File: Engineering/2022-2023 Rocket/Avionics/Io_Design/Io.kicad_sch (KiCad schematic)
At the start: 9 parts

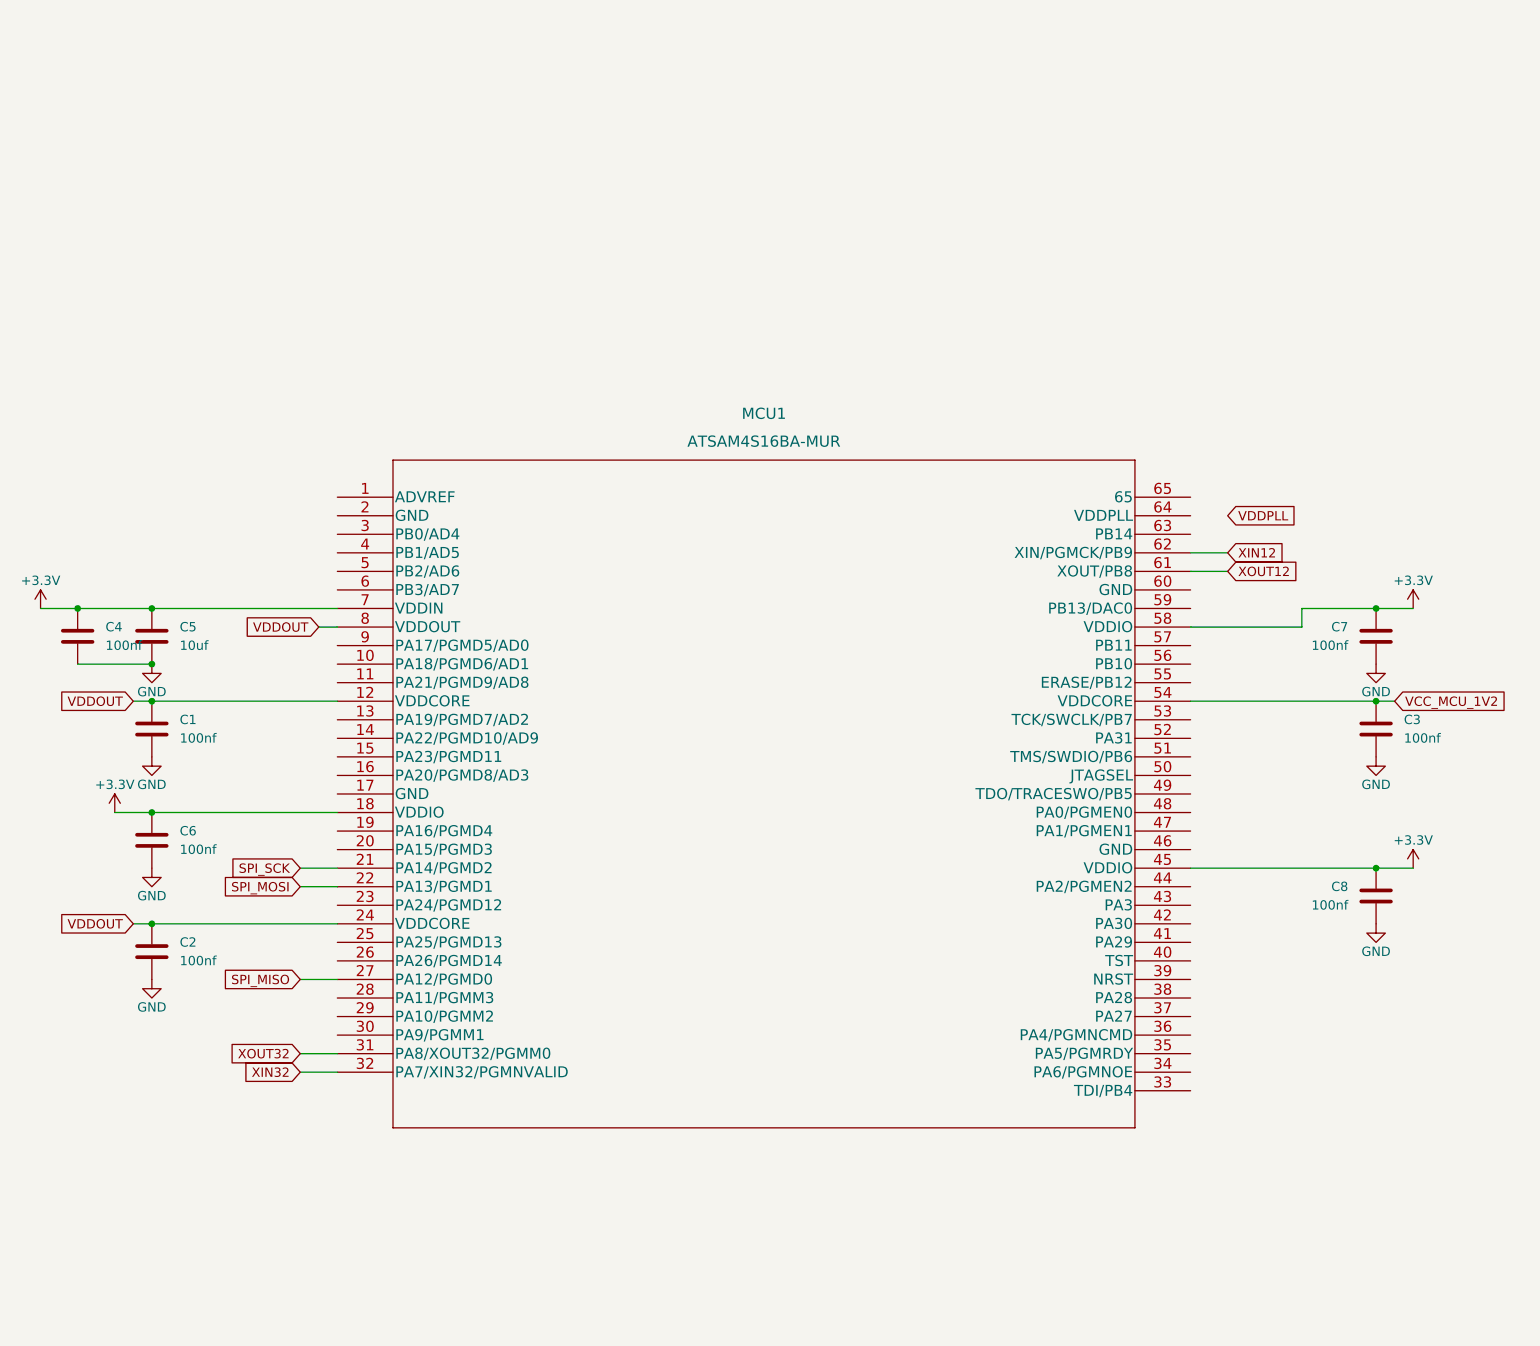
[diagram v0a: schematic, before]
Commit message: Avionics MCU switched to STM32
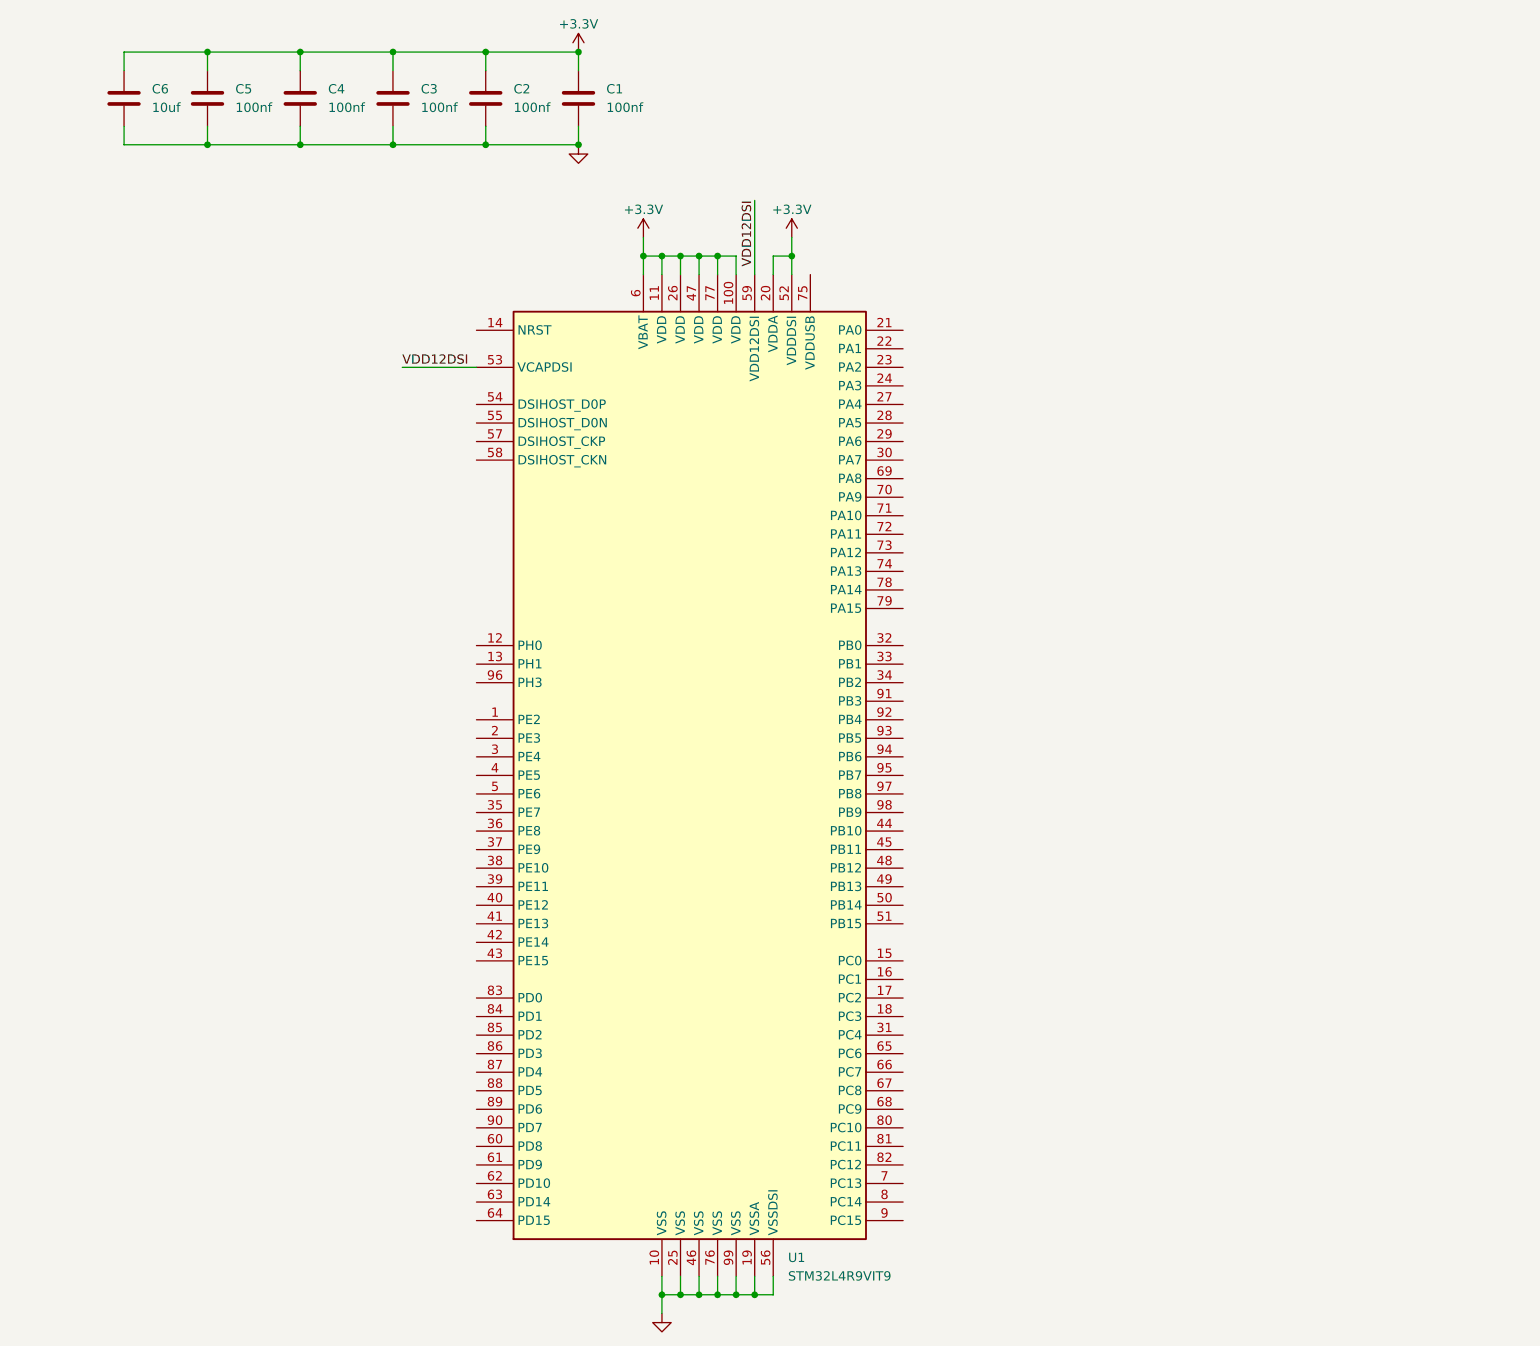
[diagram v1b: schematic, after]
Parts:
- removed C7, C8: 100nf, symbol Device:C
- removed MCU1: ATSAM4S16BA-MUR, Footprints:ATSAM4S16BA-MUR, symbol ATSAM4S16BA-MUR:ATSAM4S16BA-MUR
- added U1: STM32L4R9VIT9, Package_QFP:LQFP-100_14x14mm_P0.5mm, symbol MCU_ST_STM32L4+:STM32L4R9VITx
- C5: value 10uf -> 100nf
- C6: value 100nf -> 10uf
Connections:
- net VCC_MCU_1V2 is gone; now on net +3.3V: C3.1
- net VDDOUT is gone; now on net +3.3V: C1.1, C2.1
- net +3.3V: now also U1.100 (VDD), U1.11 (VDD), U1.20 (VDDA), U1.26 (VDD), U1.47 (VDD), U1.52 (VDDDSI), U1.6 (VBAT), U1.77 (VDD)
- net GND: now also U1.10 (VSS), U1.19 (VSSA), U1.25 (VSS), U1.46 (VSS), U1.56 (VSSDSI), U1.76 (VSS), U1.99 (VSS)
- new net VDD12DSI: U1.53 (VCAPDSI), U1.59 (VDD12DSI)

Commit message: Added 5V Regulator to schematic
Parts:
- removed C5: 100nf, symbol Device:C
- removed U1: STM32L4R9VIT9, Package_QFP:LQFP-100_14x14mm_P0.5mm, symbol MCU_ST_STM32L4+:STM32L4R9VITx
- added C? (x2): 22uf, symbol Device:C
- added C? (x2): 10pf, symbol Device:C
- added C?: 47pf, symbol Device:C
- added C?: 10uf, symbol Device:C
- added C?: 100nf, symbol Device:C
- added F1: Fuse (3A), symbol Device:Fuse
- added IC1: AP63300WU-7, SOT95P280X90-6N, symbol Io_Symbols:AP63300WU-7
- added L?: 6.8uH, symbol Device:L
- added R? (x2): 47K, symbol Device:R
- added R?: 10K, symbol Device:R
- added R?: 158K, symbol Device:R
- added R?: 30.1K, symbol Device:R
- added U1: STM32L486RGT7, Package_QFP:LQFP-64_10x10mm_P0.5mm, symbol MCU_ST_STM32L4:STM32L486RGTx
- added Y?: ECS-400-10-37B2-CKM-TR, symbol Device:Crystal_GND24
- renumbered C6 to C5
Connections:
- net GND: now also C?.2, C?.2, C?.2, IC1.4 (GND), R?.1, R?.1, R?.2, U1.1 (VBAT), U1.12 (VSSA), U1.13 (VDDA), U1.18 (VSS), U1.19 (VDD), U1.31 (VSS), U1.32 (VDD), U1.47 (VSS), U1.48 (VDDUSB), U1.63 (VSS), U1.64 (VDD)
- new net: C?.1, IC1.1 (FB), R?.1, R?.2
- new net: C?.1, F1.2, IC1.3 (VIN), R?.1
- new net: C?.1, IC1.5 (SW), L?.1
- new net: C?.2, IC1.6 (BST)
- new net: C?.2, C?.2, Y?.2, Y?.4
- new net +5V: C?.1, C?.1, C?.2, L?.2, R?.2
- new net BATT+: F1.1
- new net HSE_IN: C?.1, U1.5 (PH0), Y?.3
- new net HSE_OUT: C?.1, U1.6 (PH1), Y?.1
- new net I2C1_SCL: U1.58 (PB6)
- new net I2C1_SDA: U1.59 (PB7)
- new net I2C2_SCL: U1.29 (PB10)
- new net I2C2_SDA: U1.30 (PB11)
- new net I2C3_SCL: U1.8 (PC0)
- new net I2C3_SDA: U1.9 (PC1)
- new net SDMMC_CK: U1.53 (PC12)
- new net SDMMC_CMD: U1.54 (PD2)
- new net SDMMC_D0: U1.39 (PC8)
- new net SDMMC_D1: U1.40 (PC9)
- new net SDMMC_D2: U1.51 (PC10)
- new net SDMMC_D3: U1.52 (PC11)
- new net SDMMC_DET: U1.38 (PC7)
- new net SPI1_MISO: U1.22 (PA6)
- new net SPI1_MOSI: U1.23 (PA7)
- new net SPI1_NSS: U1.20 (PA4)
- new net SPI1_SCK: U1.21 (PA5)
- new net SPI2_MISO: U1.10 (PC2)
- new net SPI2_MOSI: U1.11 (PC3)
- new net SPI2_NSS: U1.33 (PB12)
- new net SPI2_SCK: U1.34 (PB13)
- new net SW+: R?.1, R?.2
- new net SW-: IC1.2 (EN), R?.2
- new net SWCLK: U1.49 (PA14)
- new net SWDIO: U1.46 (PA13)
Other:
- moved on the sheet: C1, C2, C3, C5

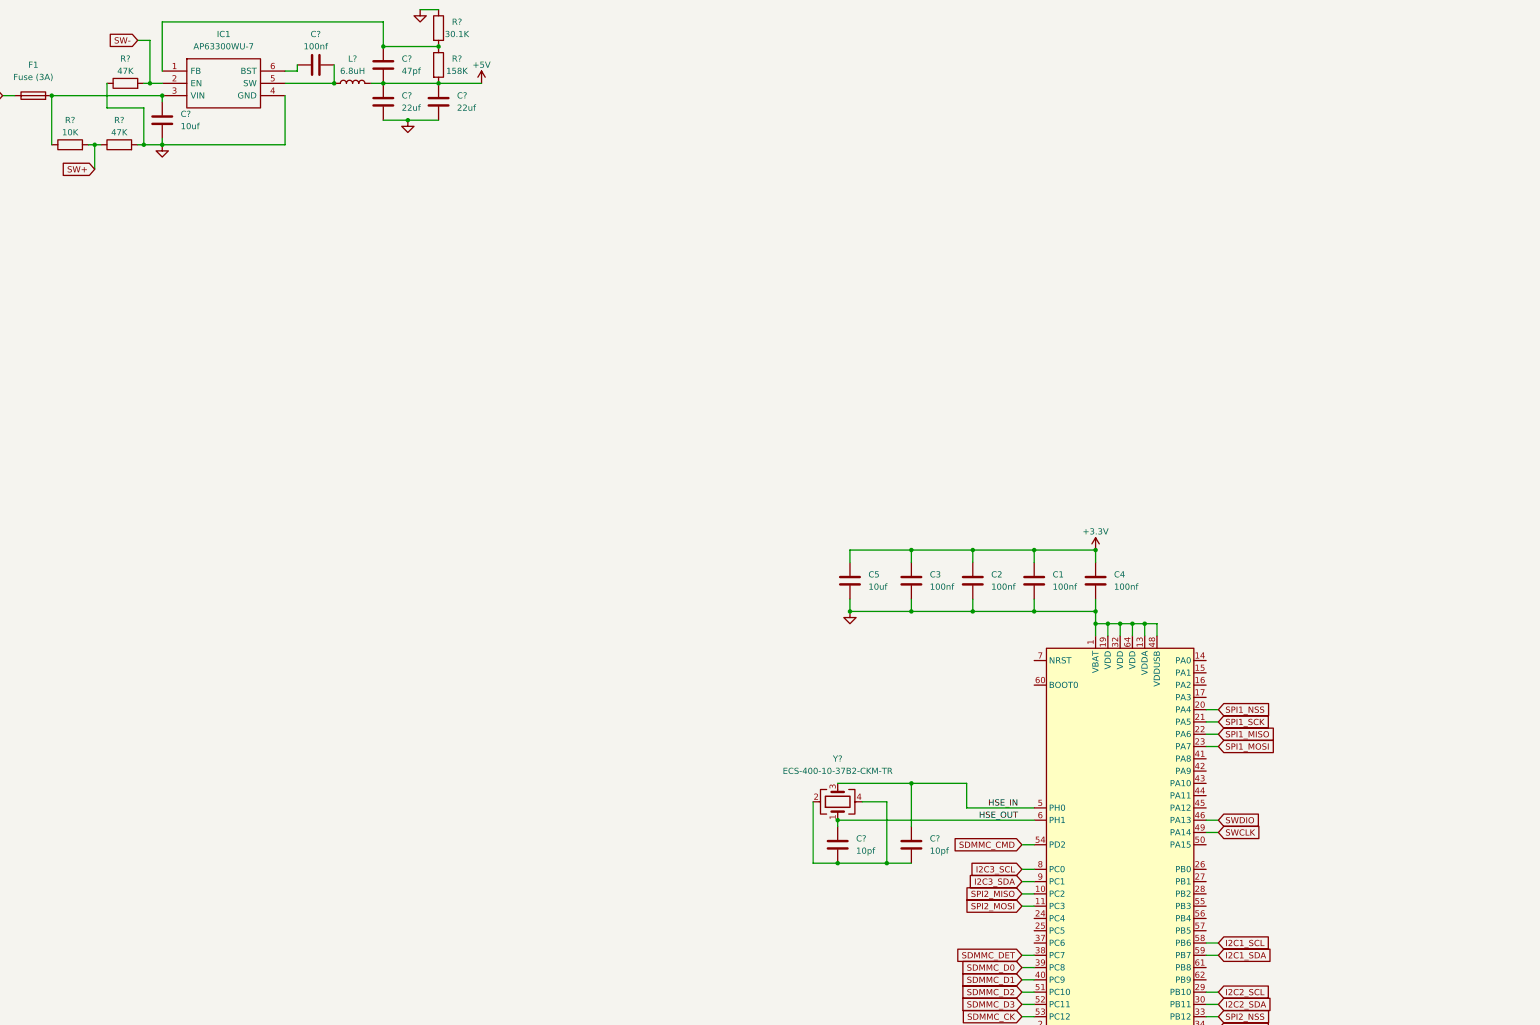
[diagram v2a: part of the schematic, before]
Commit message: Added STM32 development code and power supply
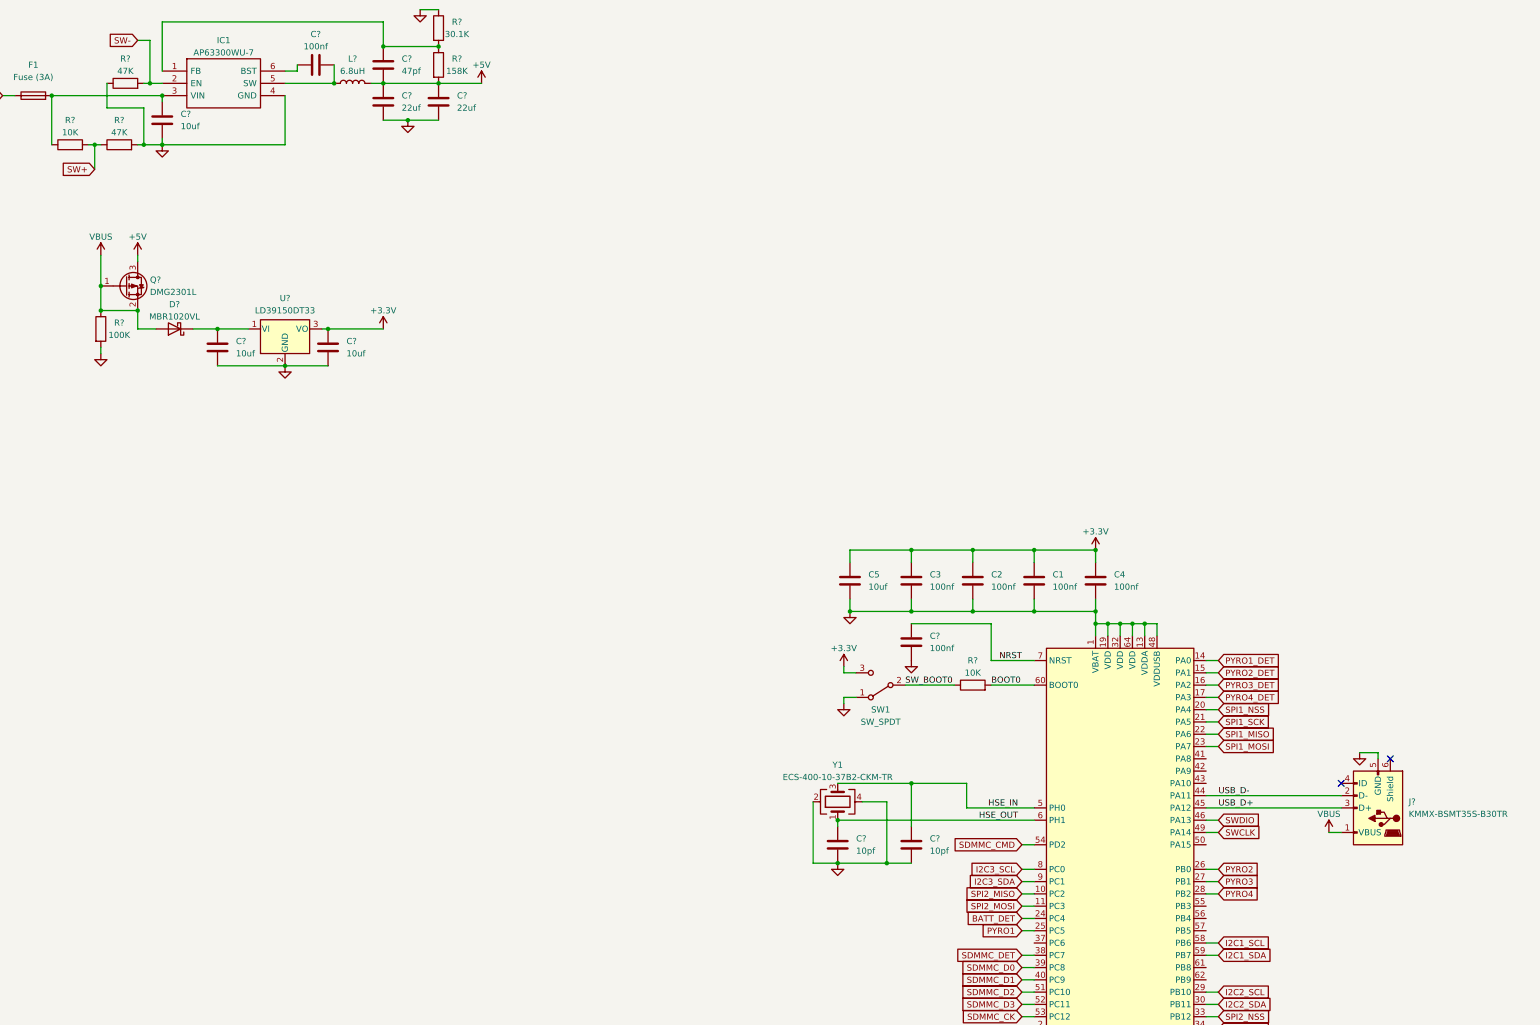
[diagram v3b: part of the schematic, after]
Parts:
- added C? (x2): 10uf, symbol Device:C
- added C?: 100nf, symbol Device:C
- added D?: MBR1020VL, Diode_SMD:D_SOD-123F, symbol Diode:MBR1020VL
- added J?: KMMX-BSMT35S-B30TR, symbol Connector:USB_B_Micro
- added Q?: DMG2301L, Package_TO_SOT_SMD:SOT-23, symbol Transistor_FET:DMG2301L
- added R?: 100K, symbol Device:R
- added R?: 10K, symbol Device:R
- added SW1: SW_SPDT, symbol Switch:SW_SPDT
- added U?: LD39150DT33, Package_TO_SOT_SMD:TO-252-3_TabPin2, symbol Regulator_Linear:LD39150DT33
- gave numbers to parts that had none: 1
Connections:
- net +3.3V: now also C?.1, SW1.3 (C), U?.3 (VO)
- net +5V: now also Q?.3 (D)
- net GND: now also C?.2, C?.2, Y1.2, Y1.4, C?.2, C?.2, C?.2, J?.5 (GND), R?.2, SW1.1 (A), U?.2 (GND)
- net PYRO1_DET: now reaches U1.14 (PA0)
- net PYRO2_DET: now reaches U1.15 (PA1)
- net PYRO3_DET: now reaches U1.16 (PA2)
- net PYRO4_DET: now reaches U1.17 (PA3)
- net BATT_DET: now reaches U1.24 (PC4)
- net PYRO1: now reaches U1.25 (PC5)
- net PYRO2: now reaches U1.26 (PB0)
- net PYRO3: now reaches U1.27 (PB1)
- net PYRO4: now reaches U1.28 (PB2)
- net USB_D-: now reaches U1.44 (PA11)
- net USB_D-: now also J?.2 (D-)
- net USB_D+: now reaches U1.45 (PA12)
- net USB_D+: now also J?.3 (D+)
- net BOOT0: now reaches U1.60 (BOOT0)
- net BOOT0: now also R?.2
- net NRST: now reaches U1.7 (NRST)
- net NRST: now also C?.1
- new net: C?.1, D?.1 (K), U?.1 (VI)
- new net SW_BOOT0: R?.1, SW1.2 (B)
- new net VBUS: D?.2 (A), J?.1 (VBUS), Q?.1 (G), Q?.2 (S), R?.1
- no-connect marks 0 -> 2
